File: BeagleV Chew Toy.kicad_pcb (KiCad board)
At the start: 2 copper layers, 52.5 x 51.7 mm, 149 parts, among them J1 Conn_02x05_Counter_Clockwise, J2 Conn_02x05_Counter_Clockwise, J3 Conn_02x05_Counter_Clockwise, U1 74HC245, U2 74HC245, U3 74HC245, U4 74HC245

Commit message: 3/4 of LEDs routed
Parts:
- C1, C2, C3, U1, U2, U3: moved to B.Cu
- moved U3 108.6 mm to (141.7, 116.7), turned to 180 degrees
- moved C3 105.6 mm to (141.4, 111.6)
- moved U4 102.6 mm to (83.8, 138.0)
- moved C4 101.6 mm to (77.0, 138.4)
- moved U2 99.6 mm to (141.7, 105.4), turned to 180 degrees
- moved C2 96.8 mm to (141.4, 100.5)
- moved U1 84.2 mm to (141.2, 88.6), turned to 180 degrees
- moved C1 82.2 mm to (141.4, 83.8)
- moved R58 34.8 mm to (179.6, 142.0)
- moved D30 28.9 mm to (176.9, 136.4)
- moved JP40 27.4 mm to (139.8, 80.8), turned to 90 degrees
- moved JP41 27.2 mm to (141.1, 80.8), turned to 0 degrees
- moved R37 10.7 mm to (161.3, 118.9), turned to 180 degrees
- moved R33 5.79 mm to (156.1, 83.3), turned to 180 degrees
- moved R54 5.36 mm to (159.9, 107.5), turned to 270 degrees
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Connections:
- BEAGLEVSIDE1 pad 11: Net-(BEAGLEVSIDE1-Pad11) -> /P11
- BEAGLEVSIDE1 pad 21: Net-(BEAGLEVSIDE1-Pad21) -> /P21
- BEAGLEVSIDE1 pad 27: Net-(BEAGLEVSIDE1-Pad27) -> /P27
- BEAGLEVSIDE1 pad 29: Net-(BEAGLEVSIDE1-Pad29) -> /P29
- BEAGLEVSIDE1 pad 3: Net-(BEAGLEVSIDE1-Pad3) -> /P3
- BEAGLEVSIDE1 pad 33: Net-(BEAGLEVSIDE1-Pad33) -> /P33
- BEAGLEVSIDE1 pad 7: Net-(BEAGLEVSIDE1-Pad7) -> /P7
- JP1 pad 2: Net-(BEAGLEVSIDE1-Pad3) -> /P3
- JP10 pad 2: Net-(BEAGLEVSIDE1-Pad27) -> /P27
- JP11 pad 2: Net-(BEAGLEVSIDE1-Pad29) -> /P29
- JP13 pad 2: Net-(BEAGLEVSIDE1-Pad33) -> /P33
- JP3 pad 2: Net-(BEAGLEVSIDE1-Pad7) -> /P7
- JP4 pad 2: Net-(BEAGLEVSIDE1-Pad11) -> /P11
- JP8 pad 2: Net-(BEAGLEVSIDE1-Pad21) -> /P21
- R1 pad 1: Net-(BEAGLEVSIDE1-Pad3) -> /P3
- R10 pad 1: Net-(BEAGLEVSIDE1-Pad27) -> /P27
- R11 pad 1: Net-(BEAGLEVSIDE1-Pad29) -> /P29
- R13 pad 1: Net-(BEAGLEVSIDE1-Pad33) -> /P33
- R3 pad 1: Net-(BEAGLEVSIDE1-Pad7) -> /P7
- R4 pad 1: Net-(BEAGLEVSIDE1-Pad11) -> /P11
- R8 pad 1: Net-(BEAGLEVSIDE1-Pad21) -> /P21
- U1 pad 11: Net-(U1-Pad11) -> /GPIO22
- U1 pad 12: Net-(U1-Pad12) -> /GPIO45
- U1 pad 13: Net-(U1-Pad13) -> /P11
- U1 pad 14: Net-(U1-Pad14) -> /GPIO13/RX
- U1 pad 15: Net-(U1-Pad15) -> /P7
- U1 pad 16: Net-(U1-Pad16) -> /GPIO14/TX
- U1 pad 17: Net-(U1-Pad17) -> /P3
- U1 pad 18: Net-(U1-Pad18) -> /GPIO47/SCL
- U1 pad 2: Net-(R29-Pad1) -> Net-(R33-Pad1)
- U1 pad 3: Net-(R30-Pad1) -> Net-(R31-Pad1)
- U1 pad 4: Net-(R31-Pad1) -> Net-(R36-Pad1)
- U1 pad 5: Net-(R32-Pad1) -> Net-(R35-Pad1)
- U1 pad 6: Net-(R33-Pad1) -> Net-(R38-Pad1)
- U1 pad 7: Net-(R34-Pad1) -> Net-(R39-Pad1)
- U1 pad 8: Net-(R35-Pad1) -> Net-(R40-Pad1)
- U1 pad 9: Net-(R36-Pad1) -> Net-(R41-Pad1)
- U2 pad 11: Net-(U2-Pad11) -> /GPIO15/CS0
- U2 pad 12: Net-(U2-Pad12) -> /GPIO11/CS1
- U2 pad 13: Net-(U2-Pad13) -> /P21
- U2 pad 14: Net-(U2-Pad14) -> /GPIO17
- U2 pad 15: Net-(U2-Pad15) -> /GPIO18/MOSI
- U2 pad 16: Net-(U2-Pad16) -> /GPIO19
- U2 pad 17: Net-(U2-Pad17) -> /GPIO20
- U2 pad 18: Net-(U2-Pad18) -> /GPIO21
- U2 pad 2: Net-(R37-Pad1) -> Net-(R44-Pad1)
- U2 pad 3: Net-(R38-Pad1) -> Net-(R43-Pad1)
- U2 pad 4: Net-(R39-Pad1) -> Net-(R46-Pad1)
- U2 pad 5: Net-(R40-Pad1) -> Net-(R47-Pad1)
- U2 pad 6: Net-(R41-Pad1) -> Net-(R50-Pad1)
- U2 pad 7: Net-(R42-Pad1) -> Net-(R49-Pad1)
- U2 pad 8: Net-(R43-Pad1) -> Net-(R54-Pad1)
- U2 pad 9: Net-(R44-Pad1) -> Net-(R52-Pad1)
- U3 pad 12: Net-(U3-Pad12) -> /GPIO7/PWM
- U3 pad 13: Net-(U3-Pad13) -> /P33
- U3 pad 14: Net-(U3-Pad14) -> /P29
- U3 pad 15: Net-(U3-Pad15) -> /GPIO6
- U3 pad 16: Net-(U3-Pad16) -> /GPIO10
- U3 pad 17: Net-(U3-Pad17) -> /P27
- U3 pad 18: Net-(U3-Pad18) -> /GPIO12/SCLK
- U3 pad 2: Net-(R45-Pad1) -> Net-(R51-Pad1)
- U3 pad 3: Net-(R46-Pad1) -> Net-(R55-Pad1)
- U3 pad 4: Net-(R47-Pad1) -> Net-(R56-Pad1)
- U3 pad 5: Net-(R48-Pad1) -> Net-(R59-Pad1)
- U3 pad 6: Net-(R49-Pad1) -> Net-(R57-Pad1)
- U3 pad 7: Net-(R50-Pad1) -> Net-(R37-Pad1)
- U3 pad 8: Net-(R51-Pad1) -> Net-(R60-Pad1)
- U3 pad 9: Net-(R52-Pad1) -> Net-(U3-Pad9)
- U4 pad 18: Net-(U4-Pad18) -> /GPIO4_TRSTN
- U4 pad 2: Net-(R53-Pad1) -> Net-(R42-Pad1)
- U4 pad 3: Net-(R54-Pad1) -> Net-(R53-Pad1)
- U4 pad 4: Net-(R55-Pad1) -> Net-(U4-Pad4)
- U4 pad 5: Net-(R56-Pad1) -> Net-(U4-Pad5)
- U4 pad 6: Net-(R57-Pad1) -> Net-(U4-Pad6)
- U4 pad 7: Net-(R58-Pad1) -> Net-(U4-Pad7)
- U4 pad 8: Net-(R59-Pad1) -> Net-(U4-Pad8)
- U4 pad 9: Net-(R60-Pad1) -> Net-(U4-Pad9)
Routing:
- net GND: track 37.4 -> 321.9 mm
- net VCC: track 0.00 -> 65.4 mm
- net /GPIO7/PWM: track 10.2 -> 35.0 mm, vias 1 -> 2
- net /GPIO6: track 12.8 -> 37.2 mm, vias 0 -> 2
- net Net-(R40-Pad1): track 0.00 -> 24.1 mm
- net /GPIO21: track 29.9 -> 50.3 mm, vias 2 -> 3
- net /GPIO10: track 14.4 -> 34.4 mm, vias 1 -> 2
- net /GPIO11/CS1: track 15.7 -> 35.2 mm, vias 1 -> 2
- net Net-(R37-Pad1): track 0.00 -> 19.3 mm
- net +3V3: track 79.9 -> 99.0 mm, vias 3 -> 4
- net /GPIO8: track 12.8 -> 31.5 mm
- net Net-(R41-Pad1): track 0.00 -> 17.6 mm
- net Net-(R54-Pad1): track 0.00 -> 17.2 mm, vias 0 -> 2
- net Net-(R33-Pad1): track 0.00 -> 17.0 mm
- net /GPIO15/CS0: track 18.5 -> 35.4 mm, vias 1 -> 2
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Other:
- board size 52.5 x 51.7 mm -> 52.6 x 51.7 mm

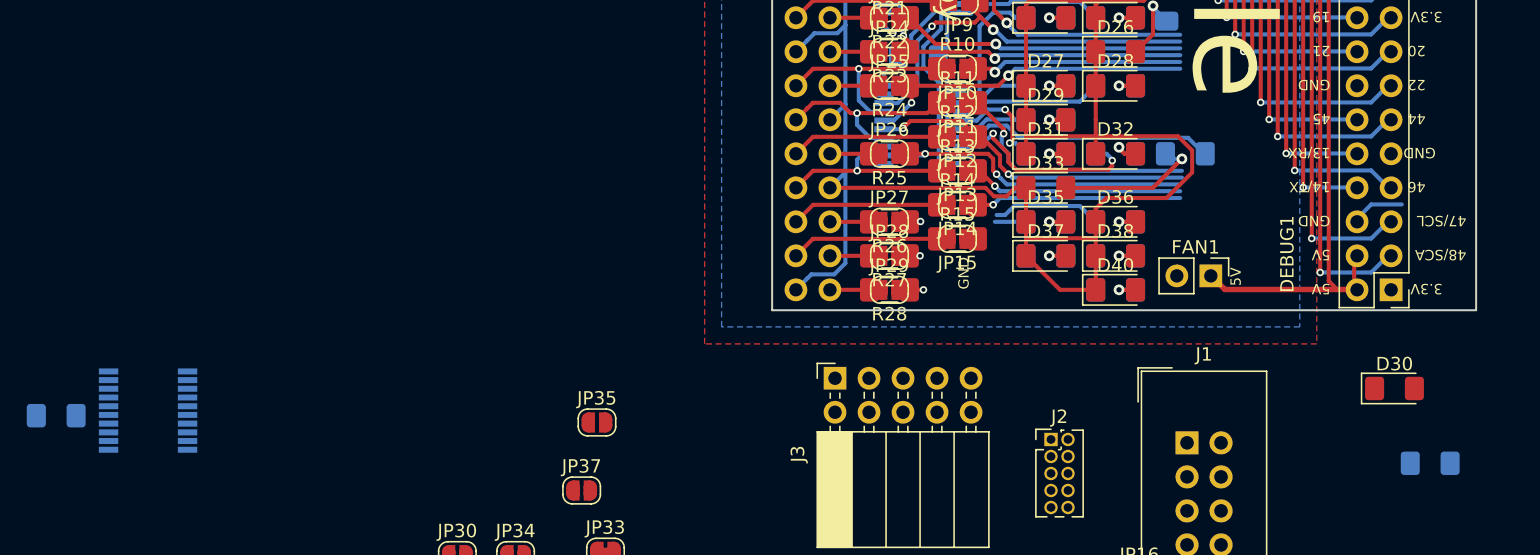
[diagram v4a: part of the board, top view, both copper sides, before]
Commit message: LEDs done
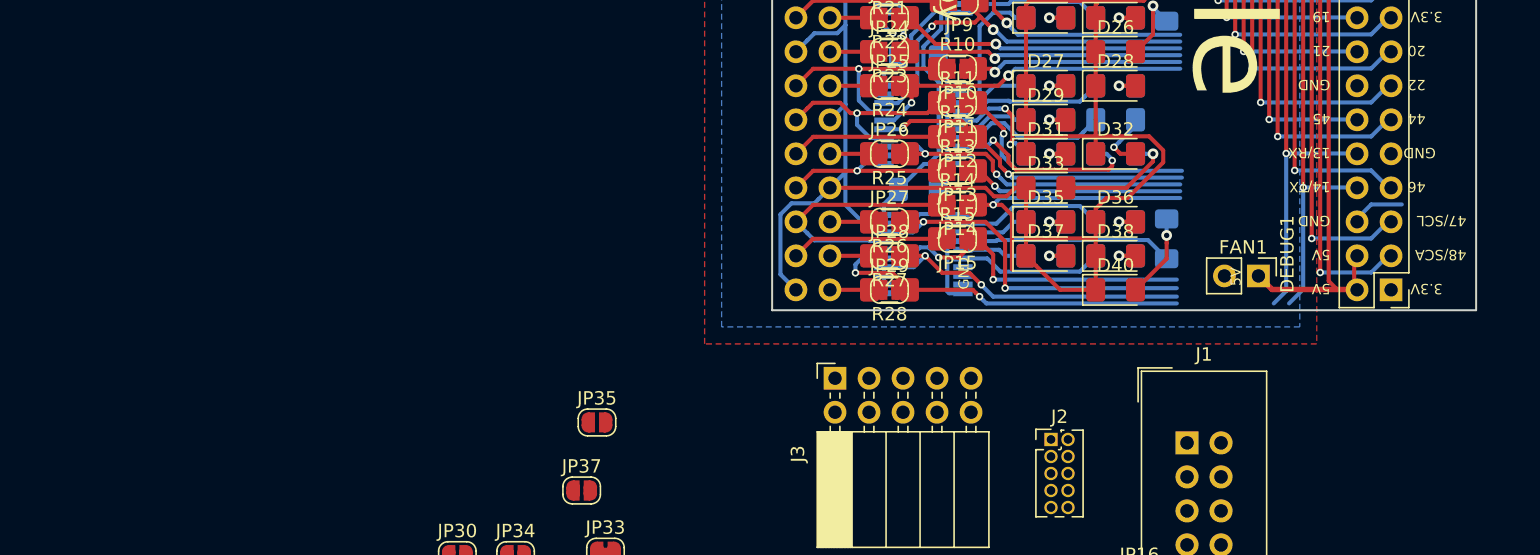
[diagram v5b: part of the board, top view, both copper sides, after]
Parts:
- removed D30: LED, LED_SMD:LED_1206_3216Metric_Pad1.42x1.75mm_HandSolder
- removed R58: 1k, Resistor_SMD:R_1206_3216Metric_Pad1.42x1.75mm_HandSolder
- moved C4 66.6 mm to (141.4, 121.5)
- moved U4 59.1 mm to (141.7, 126.4), turned to 180 degrees
- moved R32 5.39 mm to (159.9, 125.2), turned to 90 degrees
- moved R37 5.21 mm to (156.1, 118.9), turned to 0 degrees
- moved FAN1 3.56 mm to (166.8, 128.0)
- moved R60 2.54 mm to (156.1, 116.3)
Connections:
- BEAGLEVSIDE1 pad 35: Net-(BEAGLEVSIDE1-Pad35) -> /P35
- JP14 pad 2: Net-(BEAGLEVSIDE1-Pad35) -> /P35
- R14 pad 1: Net-(BEAGLEVSIDE1-Pad35) -> /P35
- U3 pad 11: Net-(U3-Pad11) -> /P33
- U3 pad 12: /GPIO7/PWM -> /P33
- U3 pad 13: /P33 -> /GPIO7/PWM
- U3 pad 7: Net-(R37-Pad1) -> Net-(R60-Pad1)
- U3 pad 8: Net-(R60-Pad1) -> Net-(R37-Pad1)
- U4 pad 11: Net-(U4-Pad11) -> /GPIO2_TDI_TO_SOC
- U4 pad 12: Net-(U4-Pad12) -> /GPIO2_TDI_TO_SOC
- U4 pad 13: Net-(U4-Pad13) -> /GPIO2_TDI_TO_SOC
- U4 pad 14: Net-(U4-Pad14) -> /GPIO2_TDI_TO_SOC
- U4 pad 15: Net-(U4-Pad15) -> /GPIO1_TCK
- U4 pad 16: Net-(U4-Pad16) -> /GPIO0_TDO_FROM_SOC
- U4 pad 17: Net-(U4-Pad17) -> /P35
- U4 pad 4: Net-(U4-Pad4) -> Net-(R32-Pad1)
- U4 pad 5: Net-(U4-Pad5) -> Net-(R45-Pad1)
- U4 pad 6: Net-(U4-Pad6) -> Net-(R48-Pad1)
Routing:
- net /GPIO0_TDO_FROM_SOC: track 1.89 -> 29.0 mm, vias 1 -> 2
- net /GPIO4_TRSTN: track 2.32 -> 28.8 mm, vias 1 -> 2
- net /GPIO2_TDI_TO_SOC: track 1.64 -> 27.5 mm, vias 1 -> 2
- net /GPIO1_TCK: track 2.63 -> 27.8 mm, vias 0 -> 2
- net /P35: track 0.00 -> 19.1 mm
- net GND: track 321.9 -> 339.6 mm
- net Net-(R32-Pad1): track 0.00 -> 15.8 mm
- net Net-(BEAGLEVSIDE1-Pad35): track 11.9 -> 0.00 mm
- net /GPIO13/RX: track 56.5 -> 68.1 mm
- net Net-(R48-Pad1): track 0.00 -> 10.8 mm
- net /GPIO14/TX: track 61.5 -> 70.6 mm
- net VCC: track 65.4 -> 71.2 mm
- net /GPIO3_TMS: track 18.0 -> 23.8 mm
- net Net-(R45-Pad1): track 0.00 -> 4.89 mm
- net Net-(R37-Pad1): track 19.3 -> 14.6 mm, vias 0 -> 2
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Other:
- board text added: "- connect UART - make 5V, 3V3, GND wider"

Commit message: ...
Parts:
- moved JP32 62.8 mm to (169.3, 145.5)
- moved JP34 61.6 mm to (172.8, 148.1), turned to 180 degrees
- moved JP35 55.9 mm to (172.8, 145.5), turned to 180 degrees
- moved JP33 51.3 mm to (169.3, 148.1)
- moved JP30 24.1 mm to (130.9, 147.2), turned to 270 degrees
- moved JP39 22.3 mm to (131.6, 161.5), turned to 270 degrees
- moved UART1 19.9 mm to (174.5, 139.3)
- moved JP31 17.9 mm to (133.5, 147.2), turned to 270 degrees
- moved JP37 17.6 mm to (126.6, 158.2), turned to 270 degrees
- moved J3 8.47 mm to (130.9, 143.0)
- moved JP16 2.47 mm to (156.5, 148.6), turned to 270 degrees
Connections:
- JP36 pad 2: Net-(JP36-Pad2) -> /GPIO14/TX
- JP37 pad 2: Net-(JP36-Pad2) -> /GPIO14/TX
- JP38 pad 2: Net-(JP38-Pad2) -> /GPIO13/RX
- JP39 pad 2: Net-(JP38-Pad2) -> /GPIO13/RX
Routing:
- net GND: track 339.6 -> 344.9 mm
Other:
- board text added: "- connect UART - make 5V, 3V3, GND wider - add silk for LEDs"
- board text removed: "- connect UART - make 5V, 3V3, GND wider"

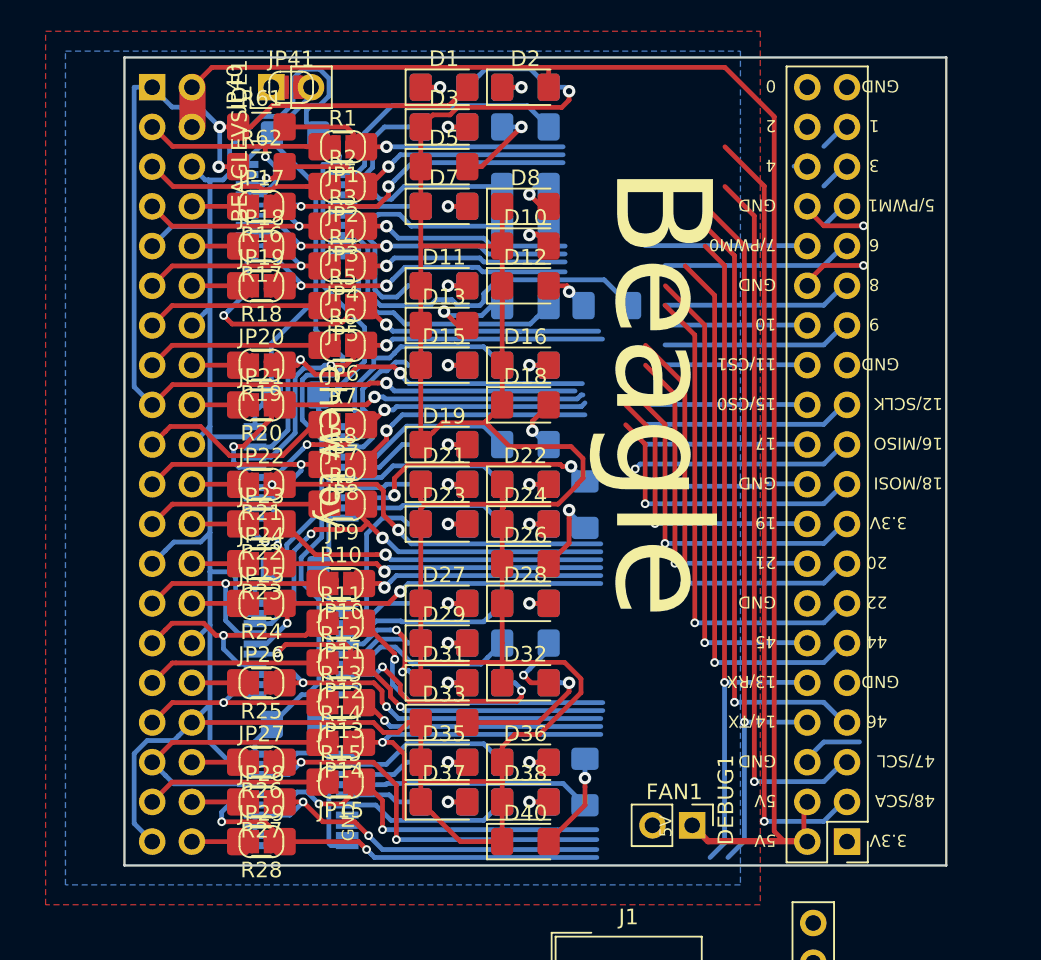
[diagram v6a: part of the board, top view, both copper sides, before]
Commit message: use elonged pads on Beagle-side header
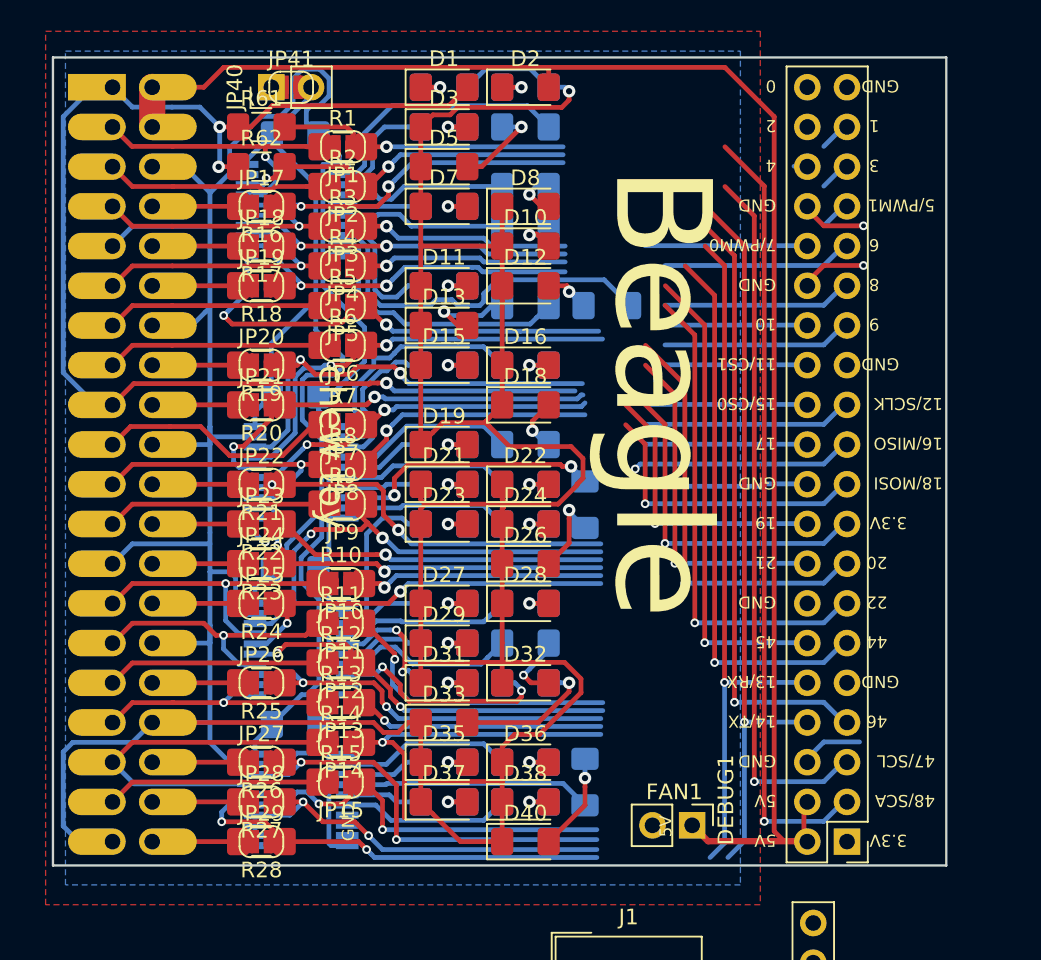
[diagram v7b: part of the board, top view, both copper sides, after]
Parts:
- BEAGLEVSIDE1: footprint Connector_PinSocket_2.54mm:PinSocket_2x20_P2.54mm_Vertical -> BeagleV Chew Toy:PinSocket_2x20_P2.54mm_Vertical_THTSMD
- moved BEAGLEVSIDE1 2.54 mm to (129.7, 80.8)
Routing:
- net GND: track 344.9 -> 359.5 mm
- net +3V3: track 99.0 -> 106.6 mm
- net /P35: track 19.1 -> 24.2 mm
- net /P33: track 14.4 -> 17.0 mm
- net Net-(BEAGLEVSIDE1-Pad31): track 11.7 -> 14.3 mm
- net Net-(BEAGLEVSIDE1-Pad23): track 11.9 -> 14.5 mm
- net /P27: track 16.5 -> 19.1 mm
- net /P21: track 16.0 -> 18.5 mm
- net /P11: track 16.3 -> 18.9 mm
- net +5V: track 100.9 -> 103.4 mm
- net /P3: track 16.8 -> 19.4 mm
- net Net-(BEAGLEVSIDE1-Pad5): track 12.2 -> 14.8 mm
- net Net-(BEAGLEVSIDE1-Pad19): track 13.5 -> 16.0 mm
- net /P7: track 15.7 -> 18.2 mm
- net Net-(BEAGLEVSIDE1-Pad15): track 12.2 -> 14.7 mm
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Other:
- board size 52.6 x 51.7 mm -> 57.2 x 51.7 mm

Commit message: main part of the PCB is done
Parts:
- moved HATSIDE1 5.72 mm to (193.2, 129.0)
- moved FAN1 4.33 mm to (162.7, 126.5), turned to 180 degrees
- moved DEBUG1 3.81 mm to (180.5, 129.0)
- moved R32 0.13 mm to (159.8, 125.2)
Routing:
- net GND: track 359.5 -> 557.6 mm, vias 3 -> 7
- net /GPIO0_TDO_FROM_SOC: track 29.0 -> 110.9 mm, vias 2 -> 3
- net /GPIO2_TDI_TO_SOC: track 27.5 -> 105.0 mm, vias 2 -> 3
- net /GPIO1_TCK: track 27.8 -> 99.2 mm, vias 2 -> 3
- net /GPIO4_TRSTN: track 28.8 -> 99.1 mm, vias 2 -> 3
- net /GPIO3_TMS: track 23.8 -> 88.5 mm, vias 1 -> 2
- net /GPIO5/PWM: track 18.4 -> 80.5 mm, vias 1 -> 2
- net /GPIO7/PWM: track 35.1 -> 82.4 mm, vias 2 -> 3
- net /GPIO6: track 37.0 -> 83.1 mm, vias 2 -> 3
- net /GPIO8: track 31.5 -> 74.8 mm, vias 1 -> 2
- net /GPIO10: track 34.4 -> 73.8 mm, vias 2 -> 3
- net +3V3: track 106.6 -> 143.3 mm
- net /GPIO9: track 28.4 -> 64.6 mm, vias 1 -> 2
- net /GPIO11/CS1: track 35.2 -> 68.7 mm, vias 2 -> 3
- net /GPIO15/CS0: track 35.4 -> 64.5 mm, vias 2 -> 3
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- added copper zone on F.Cu, net GND
- removed copper zone on F.Cu, net +3V3
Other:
- board size 57.2 x 51.7 mm -> 69.2 x 51.7 mm
- board text added: "->0 / TDO"
- board text added: "->14/TX"
- board text added: "1 kOhm (30x)"
- board text added: "100 Ohm (28x)"
- board text added: "11"
- board text added: "12"
- board text added: "13"
- board text added: "14"
- board text added: "15"
- board text added: "16"
- board text added: "18"
- board text added: "4 / TRSTRN"
- board text added: "47"
- board text added: "48"
- board text added: "5"
- board text added: "7"
- board text added: "<-13/RX"
- board text added: "<-2 / TDI"
- board text added: "BeagleV blinky toy v1 (C) 2021 snowball based on BeagleV chew toy by John 'Warthog9' Hawley CC-BY-SA 4.0 https://github.com/BBBSnowball/beaglev-chewtoy"
- board text added: "I2C, 4.7 kOhm (2x)"
- board text added: "LEDs (30x)"
- board text added: "blinky toy"
- board text added: "enable LEDs"
- board text removed: "(C) 2021 John 'Warthog9' Hawley CC-BY-SA 4.0 https://github.com/warthog9/beaglev-chewtoy v1"
- board text removed: "13/RX"
- board text removed: "14/TX"
- board text removed: "chew toy"
